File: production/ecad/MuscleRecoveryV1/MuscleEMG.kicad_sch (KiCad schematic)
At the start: 42 parts, among them J1 AudioJack3, J2 Screw_Terminal_01x03, J8 Screw_Terminal_01x07, U5 AD8232ACPZ-R7, U7 ADS1115IDGS

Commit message: saving changes
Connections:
- net LOD+: now also J8.4 (Pin_4); no longer J8.3 (Pin_3)
- net LOD-: now also J8.3 (Pin_3); no longer J8.4 (Pin_4)
- net REF: now also J8.7 (Pin_7); no longer J8.5 (Pin_5)
- net SDN: now also J8.5 (Pin_5); no longer J8.7 (Pin_7)
- net SW: now also R44.1; no longer R44.2
- net at R20.2, R21.2, R45.2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: now also R44.2; no longer R44.1
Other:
- moved on the sheet: R44
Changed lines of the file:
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@@
     )
   )
-  (global_label "LOD-" (shape input) (at 139.7 142.24 180) (fields_autoplaced)
+  (global_label "LOD-" (shape input) (at 139.7 139.7 180) (fields_autoplaced)
+    (effects (font (size 1.27 1.27)) (justify right))
+    (property "Intersheetrefs" "${INTERSHEET_REFS}" (at 131.5138 139.7 0)
+      (effects (font (size 1.27 1.27)) (justify right) hide)
+    )
+  )
+  (global_label "SW" (shape input) (at 144.78 66.04 180) (fields_autoplaced)
+    (effects (font (size 1.27 1.27)) (justify right))
+    (property "Intersheetrefs" "${INTERSHEET_REFS}" (at 139.1339 66.04 0)
+      (effects (font (size 1.27 1.27)) (justify right) hide)
+    )
+  )
+  (global_label "LA" (shape input) (at 106.68 44.45 180) (fields_autoplaced)
+    (effects (font (size 1.27 1.27)) (justify right))
+    (property "Intersheetrefs" "${INTERSHEET_REFS}" (at 101.5781 44.45 0)
+      (effects (font (size 1.27 1.27)) (justify right) hide)
+    )
+  )
+  (global_label "HP" (shape input) (at 95.25 74.93 180) (fields_autoplaced)
+    (effects (font (size 1.27 1.27)) (justify right))
+    (property "Intersheetrefs" "${INTERSHEET_REFS}" (at 89.6643 74.93 0)
+      (effects (font (size 1.27 1.27)) (justify right) hide)
+    )
+  )
+  (global_label "RL" (shape input) (at 106.68 62.23 180) (fields_autoplaced)
+    (effects (font (size 1.27 1.27)) (justify right))
+    (property "Intersheetrefs" "${INTERSHEET_REFS}" (at 101.3967 62.23 0)
+      (effects (font (size 1.27 1.27)) (justify right) hide)
+    )
+  )
+  (global_label "Vout" (shape input) (at 137.16 109.22 270) (fields_autoplaced)
+    (effects (font (size 1.27 1.27)) (justify right))
+    (property "Intersheetrefs" "${INTERSHEET_REFS}" (at 137.16 116.3175 90)
+      (effects (font (size 1.27 1.27)) (justify right) hide)
+    )
+  )
+  (global_label "LOD+" (shape input) (at 139.7 142.24 180) (fields_autoplaced)
     (effects (font (size 1.27 1.27)) (justify right))
     (property "Intersheetrefs" "${INTERSHEET_REFS}" (at 131.5138 142.24 0)
@@
     )
   )
-  (global_label "SW" (shape input) (at 144.78 66.04 180) (fields_autoplaced)
-    (effects (font (size 1.27 1.27)) (justify right))
-    (property "Intersheetrefs" "${INTERSHEET_REFS}" (at 139.1339 66.04 0)
-      (effects (font (size 1.27 1.27)) (justify right) hide)
-    )
-  )
-  (global_label "LA" (shape input) (at 106.68 44.45 180) (fields_autoplaced)
-    (effects (font (size 1.27 1.27)) (justify right))
-    (property "Intersheetrefs" "${INTERSHEET_REFS}" (at 101.5781 44.45 0)
-      (effects (font (size 1.27 1.27)) (justify right) hide)
-    )
-  )
-  (global_label "HP" (shape input) (at 95.25 74.93 180) (fields_autoplaced)
-    (effects (font (size 1.27 1.27)) (justify right))
-    (property "Intersheetrefs" "${INTERSHEET_REFS}" (at 89.6643 74.93 0)
-      (effects (font (size 1.27 1.27)) (justify right) hide)
-    )
-  )
-  (global_label "RL" (shape input) (at 106.68 62.23 180) (fields_autoplaced)
-    (effects (font (size 1.27 1.27)) (justify right))
-    (property "Intersheetrefs" "${INTERSHEET_REFS}" (at 101.3967 62.23 0)
-      (effects (font (size 1.27 1.27)) (justify right) hide)
-    )
-  )
-  (global_label "REF" (shape input) (at 138.43 144.78 180) (fields_autoplaced)
-    (effects (font (size 1.27 1.27)) (justify right))
-    (property "Intersheetrefs" "${INTERSHEET_REFS}" (at 131.9372 144.78 0)
-      (effects (font (size 1.27 1.27)) (justify right) hide)
-    )
-  )
-  (global_label "Vout" (shape input) (at 137.16 109.22 270) (fields_autoplaced)
-    (effects (font (size 1.27 1.27)) (justify right))
-    (property "Intersheetrefs" "${INTERSHEET_REFS}" (at 137.16 116.3175 90)
-      (effects (font (size 1.27 1.27)) (justify right) hide)
-    )
-  )
   (global_label "REF" (shape input) (at 115.57 82.55 180) (fields_autoplaced)
     (effects (font (size 1.27 1.27)) (justify right))
@@
     )
   )
+  (global_label "REF" (shape input) (at 138.43 149.86 180) (fields_autoplaced)
+    (effects (font (size 1.27 1.27)) (justify right))
+    (property "Intersheetrefs" "${INTERSHEET_REFS}" (at 131.9372 149.86 0)
+      (effects (font (size 1.27 1.27)) (justify right) hide)
+    )
+  )
   (global_label "RL" (shape input) (at 35.56 66.04 0) (fields_autoplaced)
     (effects (font (size 1.27 1.27)) (justify left))
@@
     )
   )
-  (global_label "LOD+" (shape input) (at 139.7 139.7 180) (fields_autoplaced)
-    (effects (font (size 1.27 1.27)) (justify right))
-    (property "Intersheetrefs" "${INTERSHEET_REFS}" (at 131.5138 139.7 0)
-      (effects (font (size 1.27 1.27)) (justify right) hide)
-    )
-  )
   (global_label "LA" (shape input) (at 35.56 63.5 0) (fields_autoplaced)
     (effects (font (size 1.27 1.27)) (justify left))
@@
     )
   )
-  (global_label "SDN" (shape input) (at 138.43 149.86 180) (fields_autoplaced)
-    (effects (font (size 1.27 1.27)) (justify right))
-    (property "Intersheetrefs" "${INTERSHEET_REFS}" (at 131.6348 149.86 0)
-      (effects (font (size 1.27 1.27)) (justify right) hide)
-    )
-  )
   (global_label "RL" (shape input) (at 41.91 96.52 0) (fields_autoplaced)
     (effects (font (size 1.27 1.27)) (justify left))
@@
     (property "Intersheetrefs" "${INTERSHEET_REFS}" (at 226.5052 77.47 0)
       (effects (font (size 1.27 1.27)) (justify left) hide)
+    )
+  )
+  (global_label "SDN" (shape input) (at 138.43 144.78 180) (fields_autoplaced)
+    (effects (font (size 1.27 1.27)) (justify right))
+    (property "Intersheetrefs" "${INTERSHEET_REFS}" (at 131.6348 144.78 0)
+      (effects (font (size 1.27 1.27)) (justify right) hide)
     )
   )
@@
     )
   )
-  (symbol (lib_id "Device:R") (at 138.43 22.86 90) (unit 1)
-    (in_bom yes) (on_board yes) (dnp no) (fields_autoplaced)
+  (symbol (lib_id "Device:R") (at 138.43 22.86 270) (mirror x) (unit 1)
+    (in_bom yes) (on_board yes) (dnp no)
     (property "Reference" "R44" (at 138.43 16.51 90)
       (effects (font (size 1.27 1.27)))

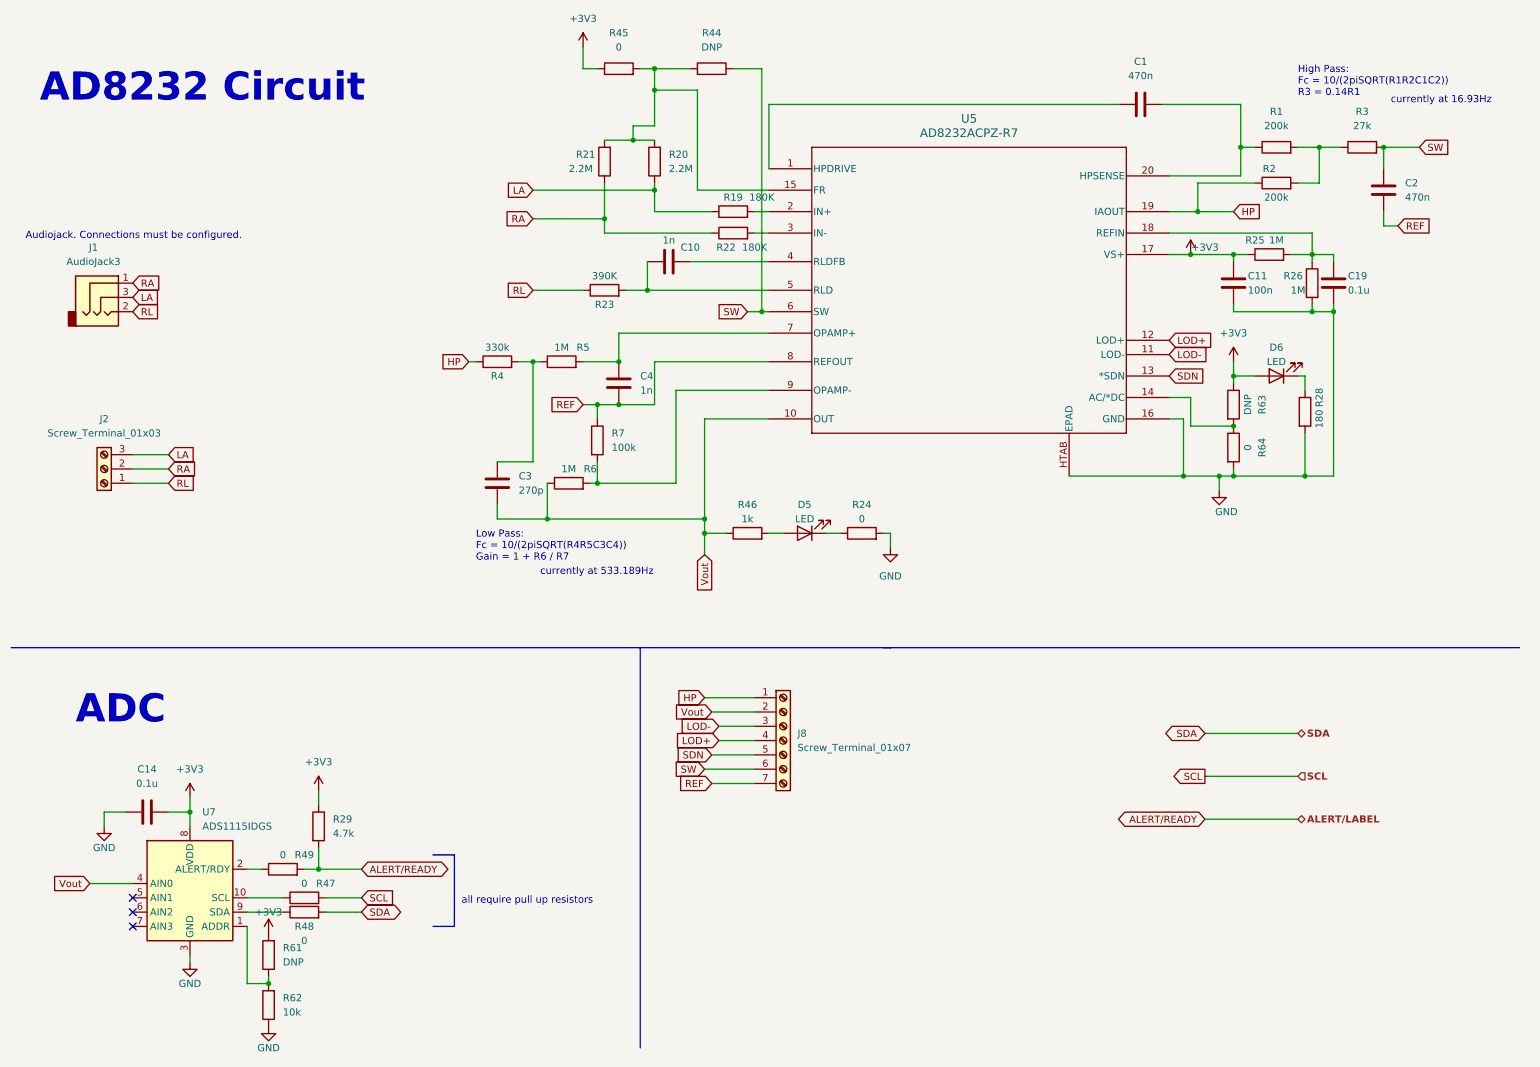
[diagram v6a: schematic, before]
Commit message: added accelerometer
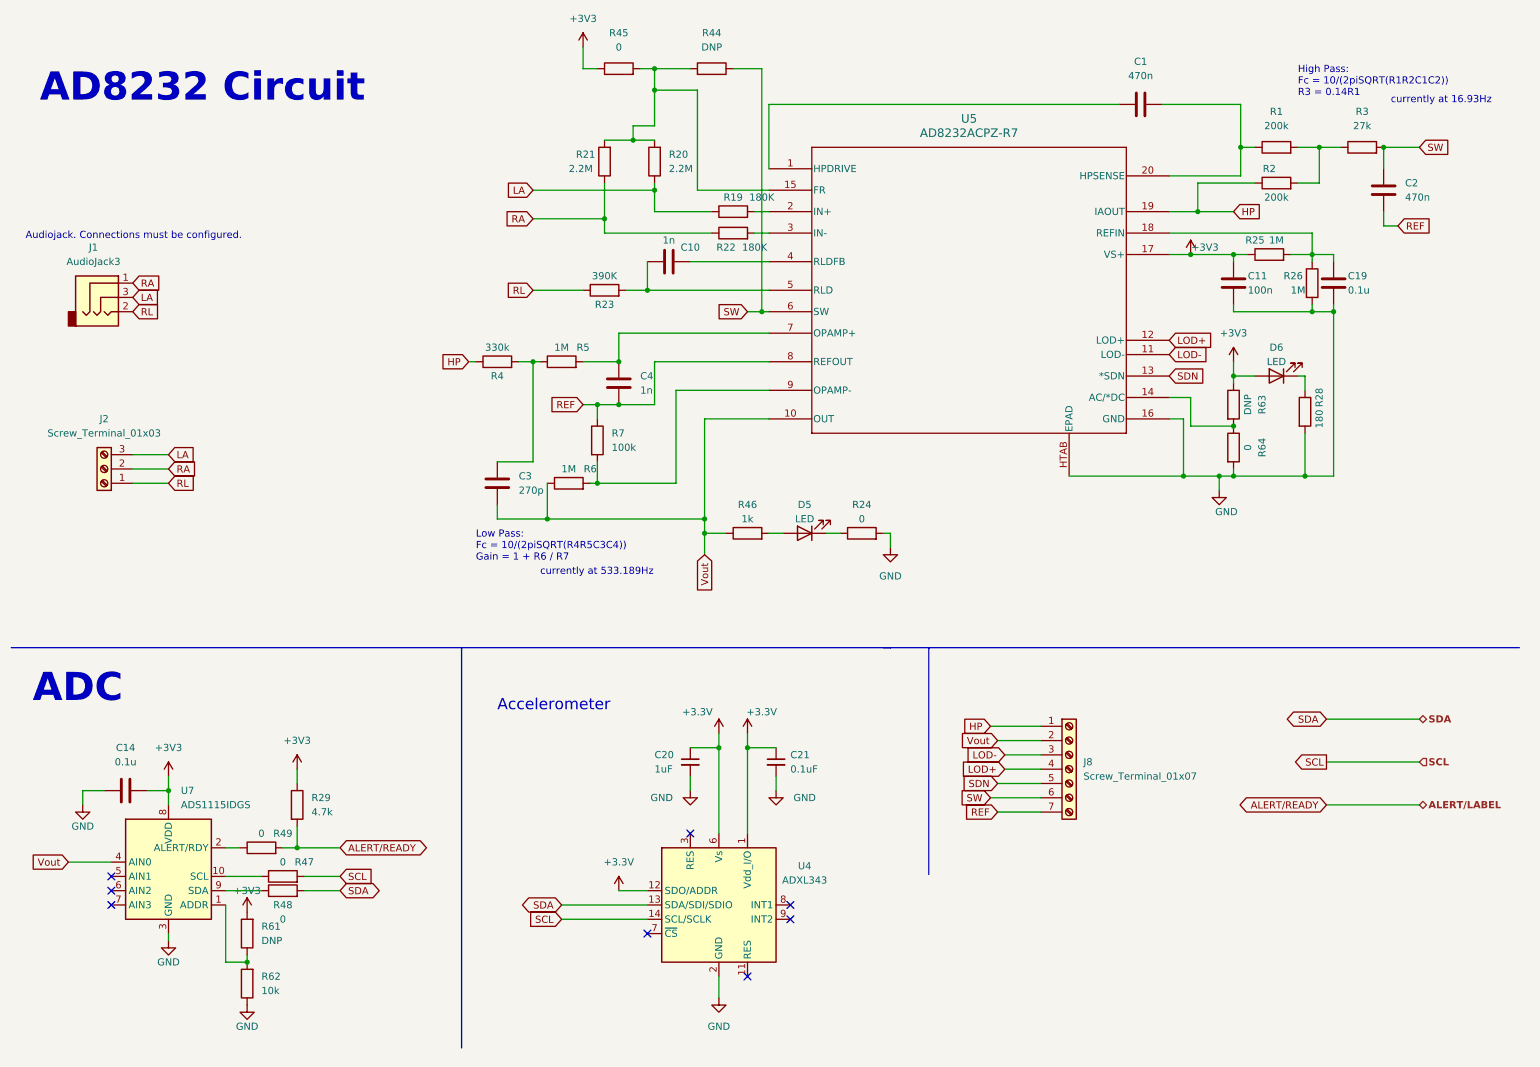
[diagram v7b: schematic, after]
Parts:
- added C20: 1uF, symbol Device:C_Small
- added C21: 0.1uF, symbol Device:C_Small
- added U4: ADXL343, Package_LGA:LGA-14_3x5mm_P0.8mm_LayoutBorder1x6y, symbol Sensor_Motion:ADXL343
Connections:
- net GND: now also C20.2, C21.2, U4.2 (GND), U4.4 (GND), U4.5 (GND)
- net SCL: now also U4.14 (SCL/SCLK)
- net SDA: now also U4.13 (SDA/SDI/SDIO)
- new net +3.3V: C20.1, C21.1, U4.1 (Vdd_I/O), U4.12 (SDO/ADDR), U4.6 (Vs)
- no-connect marks 3 -> 8
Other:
- note added: "Accelerometer"
- note removed: "all require pull up resistors"
- moved on the sheet: C14, J8, R29, R47, R48, R49, R61, R62, U7

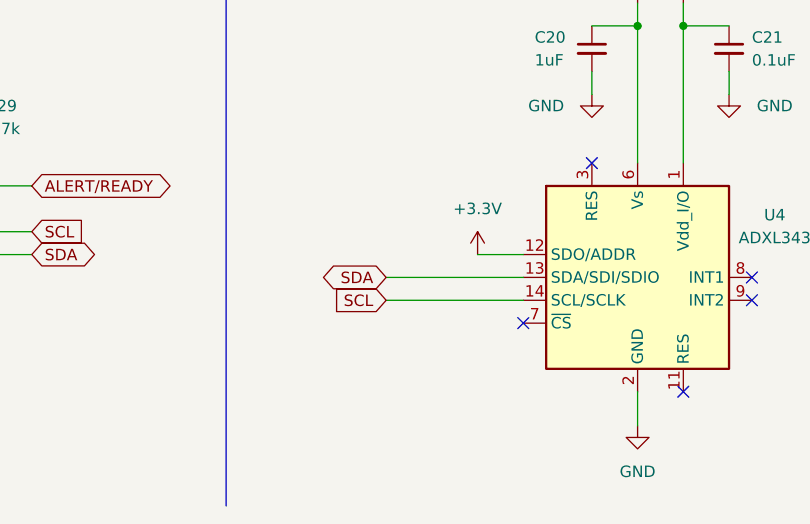
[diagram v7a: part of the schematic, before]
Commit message: 0 ohm resistors to acc
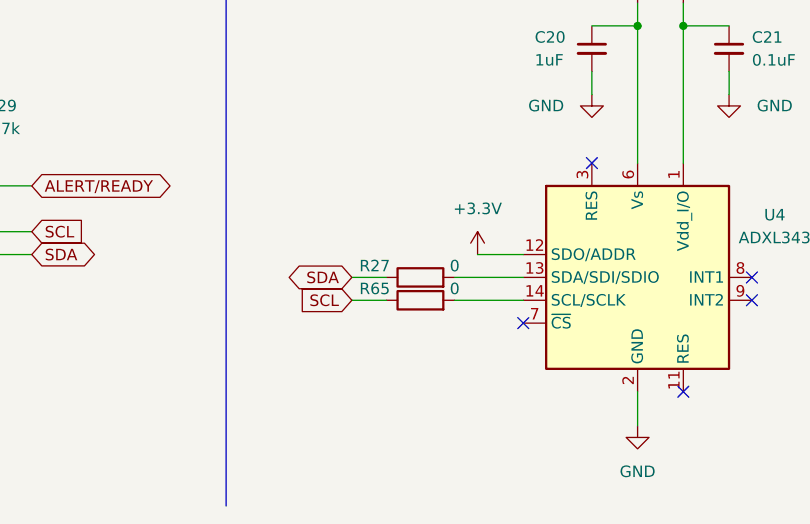
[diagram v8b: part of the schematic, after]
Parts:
- added R27, R65: 0, symbol Device:R
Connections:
- net SCL: now also R65.1; no longer U4.14 (SCL/SCLK)
- net SDA: now also R27.1; no longer U4.13 (SDA/SDI/SDIO)
- new net: R27.2, U4.13 (SDA/SDI/SDIO)
- new net: R65.2, U4.14 (SCL/SCLK)
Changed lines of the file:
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@@
+    (stroke (width 0) (type default))
+  )
+  (wire (pts (xy 119.38 171.45) (xy 127 171.45))
     (stroke (width 0) (type default))
   )
@@
     (stroke (width 0) (type default))
   )
-  (wire (pts (xy 111.76 171.45) (xy 127 171.45))
+  (wire (pts (xy 107.95 171.45) (xy 111.76 171.45))
     (stroke (width 0) (type default))
   )
@@
     (stroke (width 0) (type default))
   )
+  (wire (pts (xy 119.38 173.99) (xy 127 173.99))
+    (stroke (width 0) (type default))
+  )
   (wire (pts (xy 232.41 36.83) (xy 234.95 36.83))
     (stroke (width 0) (type default))
@@
     (stroke (width 0) (type default))
   )
-  (wire (pts (xy 111.76 173.99) (xy 127 173.99))
+  (wire (pts (xy 107.95 173.99) (xy 111.76 173.99))
     (stroke (width 0) (type default))
   )
@@
     )
   )
-  (global_label "SDA" (shape bidirectional) (at 111.76 171.45 180) (fields_autoplaced)
+  (global_label "SDA" (shape bidirectional) (at 107.95 171.45 180) (fields_autoplaced)
     (effects (font (size 1.27 1.27)) (justify right))
-    (property "Intersheetrefs" "${INTERSHEET_REFS}" (at 104.0954 171.45 0)
+    (property "Intersheetrefs" "${INTERSHEET_REFS}" (at 100.2854 171.45 0)
       (effects (font (size 1.27 1.27)) (justify right) hide)
     )
@@
     )
   )
-  (global_label "SCL" (shape input) (at 111.76 173.99 180) (fields_autoplaced)
+  (global_label "SCL" (shape input) (at 107.95 173.99 180) (fields_autoplaced)
     (effects (font (size 1.27 1.27)) (justify right))
-    (property "Intersheetrefs" "${INTERSHEET_REFS}" (at 105.2672 173.99 0)
+    (property "Intersheetrefs" "${INTERSHEET_REFS}" (at 101.4572 173.99 0)
       (effects (font (size 1.27 1.27)) (justify right) hide)
     )
@@
     )
   )
+  (symbol (lib_id "Device:R") (at 115.57 173.99 90) (unit 1)
+    (in_bom yes) (on_board yes) (dnp no)
+    (property "Reference" "R65" (at 110.49 172.72 90)
+      (effects (font (size 1.27 1.27)))
+    )
+    (property "Value" "0" (at 119.38 172.72 90)
+      (effects (font (size 1.27 1.27)))
+    )
+    (property "Footprint" "" (at 115.57 175.768 90)
+      (effects (font (size 1.27 1.27)) hide)
+    )
+    (property "Datasheet" "~" (at 115.57 173.99 0)
+      (effects (font (size 1.27 1.27)) hide)
+    )
+    (pin "1")
+    (pin "2")
+    (instances
+      (project "MuscleRecoveryV1"
+        (path "/4e550305-79d2-4e4a-a502-817ebcc79f9a/284c60dd-e199-4b03-b99f-cc7eaed256f8"
+          (reference "R65") (unit 1)
+        )
+      )
+    )
+  )
   (symbol (lib_id "Device:R") (at 243.84 83.82 0) (unit 1)
     (in_bom yes) (on_board yes) (dnp no)
@@
         )
       )
+    )
+  )
+  (symbol (lib_id "Device:R") (at 115.57 171.45 90) (unit 1)
+    (in_bom yes) (on_board yes) (dnp no)
+    (property "Reference" "R27" (at 110.49 170.18 90)
+      (effects (font (size 1.27 1.27)))
+    )
+    (property "Value" "0" (at 119.38 170.18 90)
+      (effects (font (size 1.27 1.27)))
+    )
+    (property "Footprint" "" (at 115.57 173.228 90)
+      (effects (font (size 1.27 1.27)) hide)
+    )
+    (property "Datasheet" "~" (at 115.57 171.45 0)
+      (effects (font (size 1.27 1.27)) hide)
+    )
+    (pin "2")
+    (pin "1")
+    (instances
+      (project "MuscleRecoveryV1"
+        (path "/4e550305-79d2-4e4a-a502-817ebcc79f9a/284c60dd-e199-4b03-b99f-cc7eaed256f8"
+          (reference "R27") (unit 1)
+        )
+      )
